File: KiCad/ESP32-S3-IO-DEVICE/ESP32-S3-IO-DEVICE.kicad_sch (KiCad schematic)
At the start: 62 parts, among them J1 Terminal_04, J2 Terminal_04, J3 Terminal_06, J4 Terminal_02, J5 Terminal_04, J6 Terminal_06, Q1 2SC1815, Q10 2SC1815, Q11 2SC1815, Q12 2SC1815, Q2 2SC1815, Q3 2SC1815, Q4 2SC1815, Q5 2SC1815, Q6 2SC1815, Q7 2SC1815, Q8 2SC1815, Q9 2SC1815, U1 ESP32-S3-DevKitC

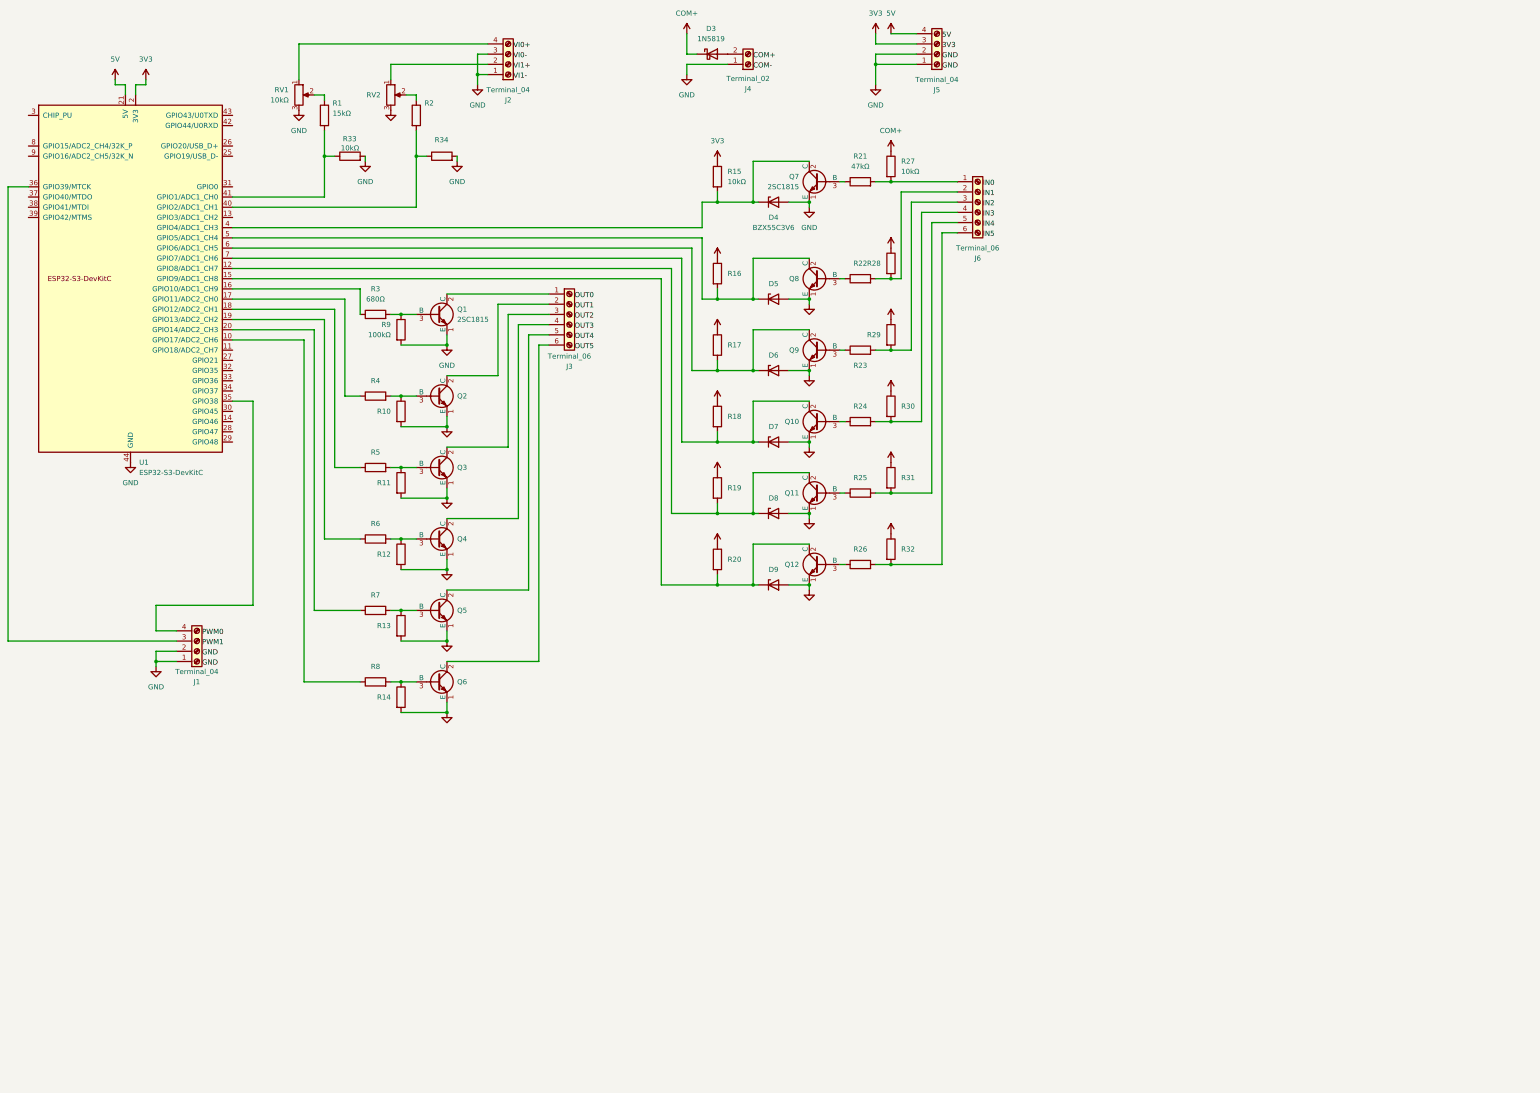
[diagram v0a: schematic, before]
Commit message: Prepare ESP32IO for public release
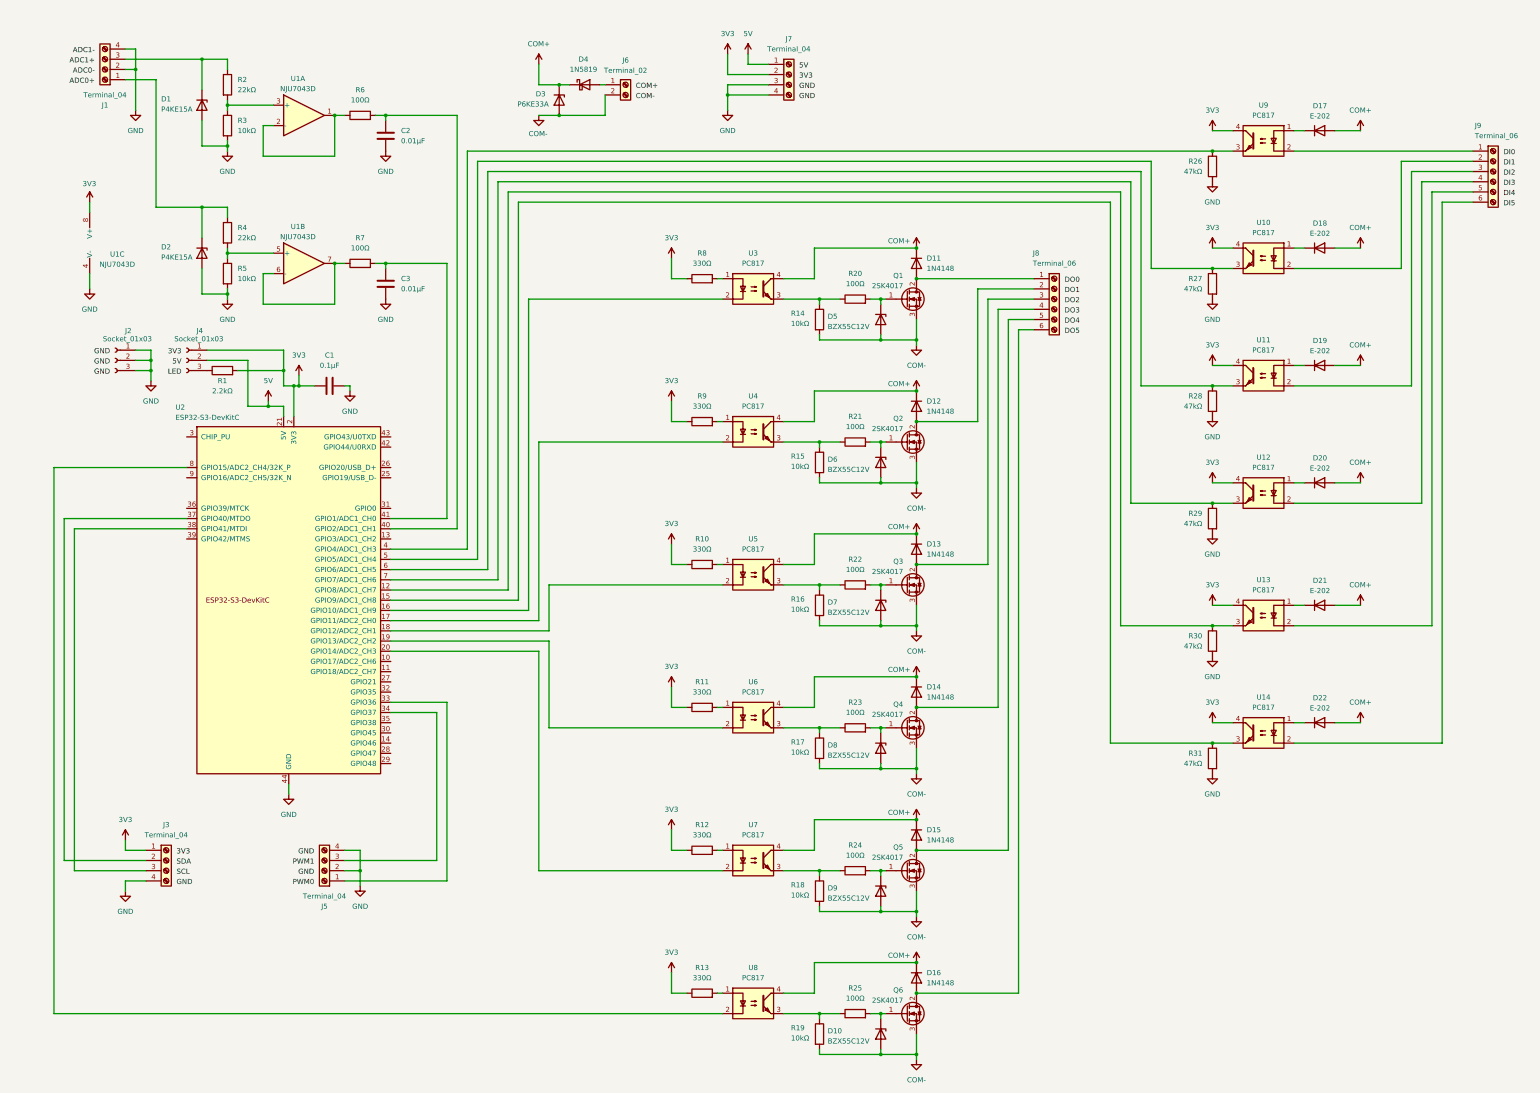
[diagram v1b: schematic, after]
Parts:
- removed D3: 1N5819, Diode_THT:D_DO-41_SOD81_P10.16mm_Horizontal, symbol Diode:1N5819
- removed D4: BZX55C3V6, Diode_THT:D_DO-35_SOD27_P7.62mm_Horizontal, symbol Device:D_Zener
- removed J1: Terminal_04, TerminalBlock_Phoenix:TerminalBlock_Phoenix_MKDS-1,5-4-5.08_1x04_P5.08mm_Horizontal, symbol Connector:Screw_Terminal_01x04
- removed J3, J6: Terminal_06, TerminalBlock_Phoenix:TerminalBlock_Phoenix_MKDS-1,5-6-5.08_1x06_P5.08mm_Horizontal, symbol Connector:Screw_Terminal_01x06
- removed Q1, Q10, Q11, Q12, Q2, Q3, Q4, Q5, Q6, Q7, Q8, Q9: 2SC1815, Package_TO_SOT_THT:TO-92_Inline, symbol Transistor_BJT:2SC1815
- removed R32, R33: 10kΩ, Resistor_THT:R_Axial_DIN0207_L6.3mm_D2.5mm_P7.62mm_Horizontal, symbol Device:R
- removed R34: 15kΩ, Resistor_THT:R_Axial_DIN0207_L6.3mm_D2.5mm_P7.62mm_Horizontal, symbol Device:R
- removed RV1, RV2: 10kΩ, Potentiometer_THT:Potentiometer_Bourns_3386P_Vertical, symbol Device:R_Potentiometer
- removed U1: ESP32-S3-DevKitC, Espressif:ESP32-S3-DevKitC-1, symbol Espressif:ESP32-S3-DevKitC
- added C1: 0.1μF, Capacitor_THT:C_Disc_D3.0mm_W1.6mm_P2.50mm, symbol Device:C
- added C2, C3: 0.01μF, Capacitor_THT:C_Disc_D3.0mm_W1.6mm_P2.50mm, symbol Device:C
- added D1, D2: P4KE15A, Diode_THT:D_A-405_P7.62mm_Horizontal, symbol Device:D_Zener
- added D10: BZX55C12V, Diode_THT:D_DO-35_SOD27_P7.62mm_Horizontal, symbol Device:D_Zener
- added D11, D12, D13, D14, D15, D16: 1N4148, Diode_THT:D_DO-35_SOD27_P7.62mm_Horizontal, symbol Diode:1N4148
- added D17, D18, D19, D20, D21, D22: E-202, Diode_THT:D_DO-35_SOD27_P7.62mm_Horizontal, symbol Device:D
- added D3: P6KE33A, Diode_THT:D_A-405_P7.62mm_Horizontal, symbol Device:D_Zener
- added D4: 1N5819, Diode_THT:D_DO-41_SOD81_P7.62mm_Horizontal, symbol Diode:1N5819
- added J2, J4: Socket_01x03, Connector_PinSocket_2.54mm:PinSocket_1x03_P2.54mm_Vertical, symbol Connector:Conn_01x03_Socket
- added J3, J5: Terminal_04, TerminalBlock_Phoenix:TerminalBlock_Phoenix_MKDS-1,5-4-5.08_1x04_P5.08mm_Horizontal, symbol Connector:Screw_Terminal_01x04
- added J8, J9: Terminal_06, TerminalBlock_Phoenix:TerminalBlock_Phoenix_MKDS-1,5-6-5.08_1x06_P5.08mm_Horizontal, symbol Connector:Screw_Terminal_01x06
- added Q1, Q2, Q3, Q4, Q5, Q6: 2SK4017, Package_TO_SOT_THT:TO-126-3_Vertical, symbol Transistor_FET:Q_NMOS_GDS
- added U1: NJU7043D, Package_DIP:DIP-8_W7.62mm, symbol Amplifier_Operational:MCP6002-xP
- added U10, U11, U12, U13, U14, U3, U4, U5, U6, U7, U8, U9: PC817, Package_DIP:DIP-4_W7.62mm, symbol Isolator:PC817
- added U2: ESP32-S3-DevKitC, Espressif:ESP32-S3-DevKitC_3rd_party, symbol Espressif:ESP32-S3-DevKitC
- D5, D6, D7, D8, D9: value BZX55C3V6 -> BZX55C12V
- R1: value 15kΩ -> 2.2kΩ
- R10, R11, R12, R13, R9: value 100kΩ -> 330Ω
- R14: value 100kΩ -> 10kΩ
- R2: value 10kΩ -> 22kΩ
- R20: value 10kΩ -> 100Ω
- R21, R22, R23, R24, R25: value 47kΩ -> 100Ω
- R27, R28, R29, R30, R31: value 10kΩ -> 47kΩ
- R3, R5: value 680Ω -> 10kΩ
- R4: value 680Ω -> 22kΩ
- R6, R7: value 680Ω -> 100Ω
- R8: value 680Ω -> 330Ω
- renumbered J2 to J1, J4 to J6, J5 to J7
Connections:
- net 3V3: now also J7.2 (Pin_2), R1.2, R10.1, R11.1, R12.1, R13.1, R8.1, R9.1, C1.1, J3.1 (Pin_1), J4.1 (Pin_1), U1.8 (V+), U10.4, U11.4, U12.4, U13.4, U14.4, U2.1 (3V3), U2.2 (3V3), U9.4; no longer J7.3 (Pin_3), R15.1, R16.1, R17.1, R18.1, R19.1, R20.1
- net 5V: now also J7.1 (Pin_1), J4.2 (Pin_2), U2.21 (5V); no longer J7.4 (Pin_4)
- net COM+: now also D11.1 (K), D12.1 (K), D13.1 (K), D14.1 (K), D15.1 (K), D16.1 (K), D17.2 (A), D18.2 (A), D19.2 (A), D20.2 (A), D21.2 (A), D22.2 (A), D3.1 (K), D4.1 (K), U3.4, U4.4, U5.4, U6.4, U7.4, U8.4; no longer R27.1, R28.1, R29.1, R30.1, R31.1
- net COM-: now also D5.2 (A), D6.2 (A), D7.2 (A), D8.2 (A), D9.2 (A), J6.2 (Pin_2), R14.2, R15.2, R16.2, R17.2, R18.2, R19.2, D10.2 (A), D3.2 (A), Q1.3 (S), Q2.3 (S), Q3.3 (S), Q4.3 (S), Q5.3 (S), Q6.3 (S)
- net GND: now also J1.2 (Pin_2), J1.4 (Pin_4), J7.3 (Pin_3), J7.4 (Pin_4), R26.2, R27.2, R28.2, R29.2, R3.2, R30.2, R31.2, R5.2, C1.2, C2.2, C3.2, D1.2 (A), D2.2 (A), J2.1 (Pin_1), J2.2 (Pin_2), J2.3 (Pin_3), J3.4 (Pin_4), J5.2 (Pin_2), J5.4 (Pin_4), U1.4 (V-), U2.22 (GND), U2.23 (GND), U2.24 (GND), U2.44 (GND); no longer D5.2 (A), D6.2 (A), D7.2 (A), D8.2 (A), D9.2 (A), J1.1 (Pin_1), J1.3 (Pin_3), J6.1 (Pin_1), J7.1 (Pin_1), J7.2 (Pin_2), R10.2, R11.2, R12.2, R13.2, R14.2, R9.2
- net at R22.1: now also R16.1, U5.3
- net at R22.2: now also D7.1 (K), Q3.1 (G); no longer R28.2
- net at R25.1: now also R19.1, U8.3
- net at R25.2: now also D10.1 (K), Q6.1 (G); no longer R31.2
- net at R24.2: now also D9.1 (K), Q5.1 (G); no longer R30.2
- net at R24.1: now also R18.1, U7.3
- net at D8.1 (K): now also R23.2, Q4.1 (G); no longer R19.2
- net at R1.1: now also J4.3 (Pin_3)
- net at R3.1: now also R2.2, U1.3 (+)
- net at R20.2: now also D5.1 (K), Q1.1 (G); no longer D9.1 (K)
- net at D6.1 (K): now also R21.2, Q2.1 (G); no longer R17.2
- net at R23.1: now also R17.1, U6.3
- net at R21.1: now also R15.1, U4.3
- net at R2.1: now also J1.3 (Pin_3), D1.1 (K)
- net at R5.1: now also R4.2, U1.5 (+)
- net at R26.1: now also U2.4 (GPIO4/ADC1_CH3), U9.3
- net at R7.2: now also C3.1, U2.41 (GPIO1/ADC1_CH0); no longer R13.1
- net at R4.1: now also J1.1 (Pin_1), D2.1 (K)
- net at R8.2: now also U3.1; no longer R14.1
- net at R6.2: now also C2.1, U2.40 (GPIO2/ADC1_CH1); no longer R12.1
- net at R6.1: now also U1.1, U1.2 (-)
- net at R7.1: now also U1.6 (-), U1.7
- new net: R12.2, U7.1
- new net: D15.2 (A), J8.5 (Pin_5), Q5.2 (D)
- new net: D20.1 (K), U12.1
- new net: J9.4 (Pin_4), U12.2
- new net: R29.1, U12.3, U2.7 (GPIO7/ADC1_CH6)
- new net: D21.1 (K), U13.1
- new net: J9.5 (Pin_5), U13.2
- new net: R30.1, U13.3, U2.12 (GPIO8/ADC1_CH7)
- new net: D13.2 (A), J8.3 (Pin_3), Q3.2 (D)
- new net: R31.1, U14.3, U2.15 (GPIO9/ADC1_CH8)
- new net: U2.16 (GPIO10/ADC1_CH9), U3.2
- new net: U2.17 (GPIO11/ADC2_CH0), U4.2
- new net: U2.18 (GPIO12/ADC2_CH1), U5.2
- new net: U2.19 (GPIO13/ADC2_CH2), U6.2
- new net: U2.20 (GPIO14/ADC2_CH3), U7.2
- new net: J5.1 (Pin_1), U2.33 (GPIO36)
- new net: J5.3 (Pin_3), U2.34 (GPIO37)
- new net: J3.2 (Pin_2), U2.37 (GPIO40/MTDO)
- new net: J3.3 (Pin_3), U2.38 (GPIO41/MTDI)
- new net: R27.1, U10.3, U2.5 (GPIO5/ADC1_CH4)
- new net: R28.1, U11.3, U2.6 (GPIO6/ADC1_CH5)
- new net: U2.8 (GPIO15/ADC2_CH4/32K_P), U8.2
- new net: D17.1 (K), U9.1
- new net: J9.1 (Pin_1), U9.2
- new net: R9.2, U4.1
- new net: D14.2 (A), J8.4 (Pin_4), Q4.2 (D)
- new net: D18.1 (K), U10.1
- new net: R11.2, U6.1
- new net: J9.2 (Pin_2), U10.2
- new net: J9.3 (Pin_3), U11.2
- new net: J9.6 (Pin_6), U14.2
- new net: R13.2, U8.1
- new net: D19.1 (K), U11.1
- new net: D22.1 (K), U14.1
- new net: D11.2 (A), J8.1 (Pin_1), Q1.2 (D)
- new net: D12.2 (A), J8.2 (Pin_2), Q2.2 (D)
- new net: D16.2 (A), J8.6 (Pin_6), Q6.2 (D)
- new net: R14.1, R20.1, U3.3
- new net: D4.2 (A), J6.1 (Pin_1)
- new net: R10.2, U5.1
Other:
- moved on the sheet: J1, J6, J7
